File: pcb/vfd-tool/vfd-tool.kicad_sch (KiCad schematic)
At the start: 169 parts, among them J1 Conn_ARM_SWD_TagConnect_TC203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, J2 USB_C_Receptacle_USB2.0, J3 Micro_SD_Card, J4 Conn_01x10, J5 Raspberry_Pi_2_3, J6 Conn_02x15_Odd_Even, J7 Conn_02x15_Odd_Even, J8 Conn_02x08_Odd_Even, J9 Conn_01x02_Socket, SW1 SW_Push, SW2 SW_Push, U1 RP2040, U10 TPS54331DR, U11 BQ24075RGT, U2 USB2514B_M2, U3 SRV05-4, U4 FUSB302BMPX, U5 PCF85263AT, U6 W25Q32JVSS, U7 TPS562200, U8 TPS562200, U9 MAX17048G_T10, Y1 24MHz, Y2 24MHz, Y3 32.768kHz

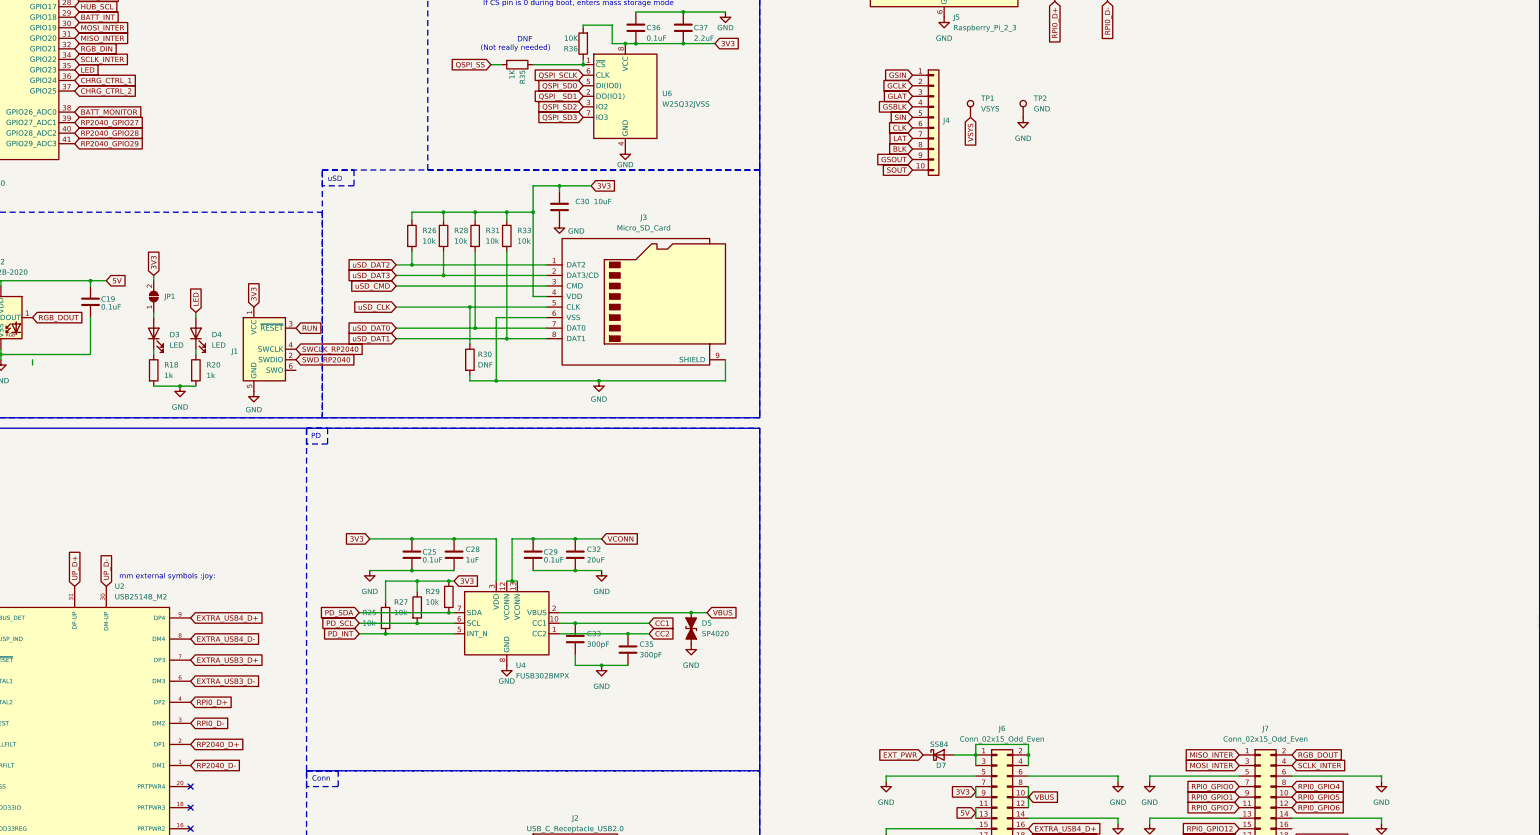
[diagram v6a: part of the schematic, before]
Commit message: DRC Fixed and added solder jumpers
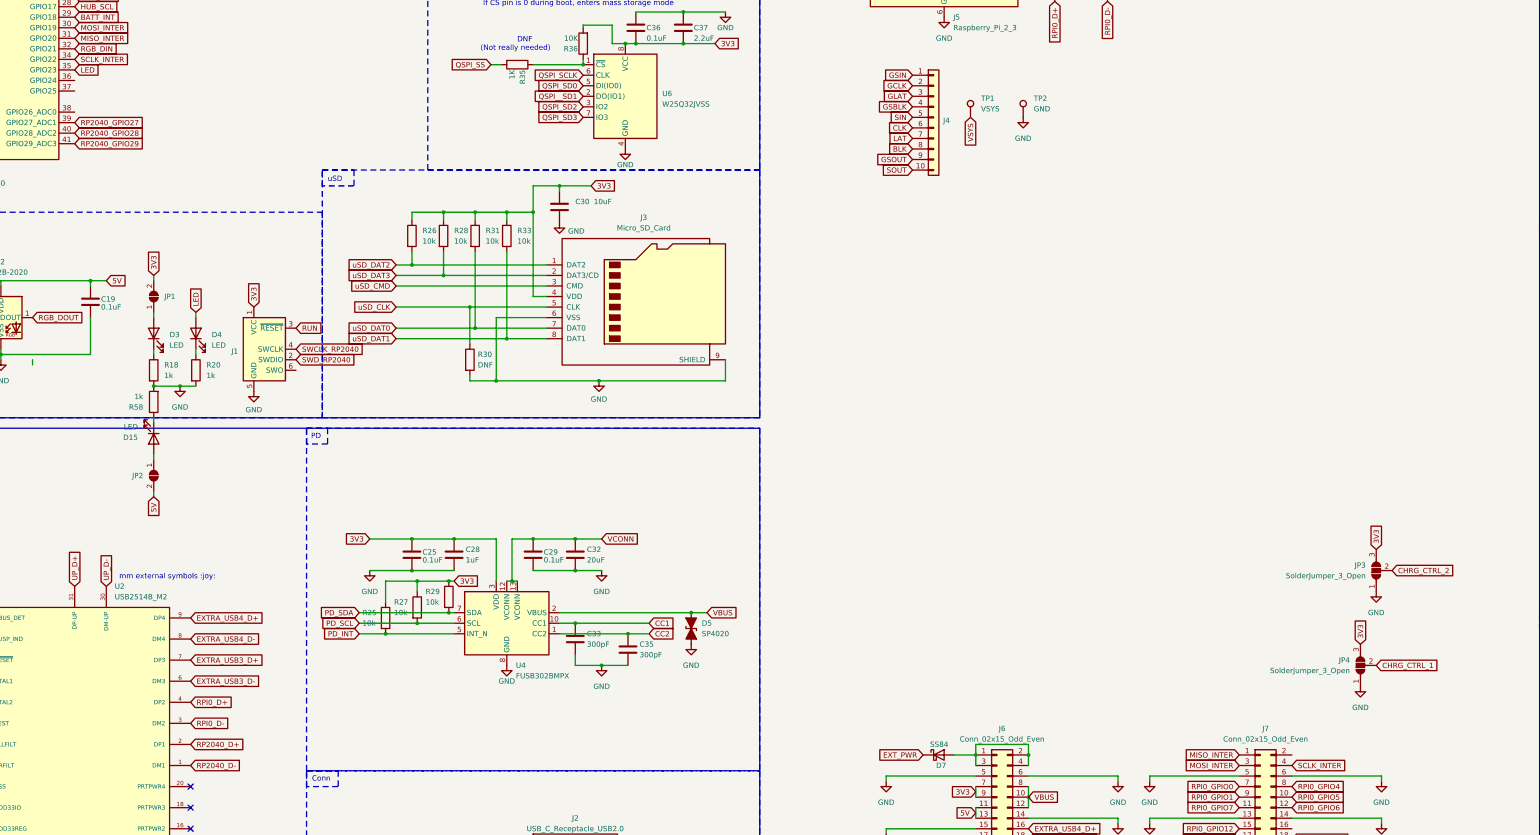
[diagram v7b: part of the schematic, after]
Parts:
- added D15: LED, LED_SMD:LED_0603_1608Metric, symbol Device:LED
- added JP2: SolderJumper_2_Open, Jumper:SolderJumper-2_P1.3mm_Open_TrianglePad1.0x1.5mm, symbol Jumper:SolderJumper_2_Open
- added JP3, JP4: SolderJumper_3_Open, Jumper:SolderJumper-3_P2.0mm_Open_TrianglePad1.0x1.5mm, symbol Jumper:SolderJumper_3_Open
- added R58: 1k, Resistor_SMD:R_0402_1005Metric, symbol Device:R
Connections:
- net 3V3: now also JP3.3 (B), JP4.3 (B)
- net 5V: now also JP2.2 (B)
- net BATT_MONITOR: no longer U1.38 (GPIO26_ADC0)
- net CHRG_CTRL_1: now also JP4.2 (C); no longer U1.36 (GPIO24)
- net CHRG_CTRL_2: now also JP3.2 (C); no longer U1.37 (GPIO25)
- net GND: now also JP3.1 (A), JP4.1 (A), R58.2
- net RGB_DOUT: no longer J7.2 (Pin_2)
- new net: D15.1 (K), R58.1
- new net: D15.2 (A), JP2.1 (A)

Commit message: fix #1 and #2
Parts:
- D11: value LED -> Blue
- D12, D15, D3: value LED -> Green
- D4: value LED -> Purple
- Y3: value 32.768kHz -> 32.768kHz
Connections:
- net GND: now also D10.2 (A), D5.2 (A2); no longer D10.1 (K), D5.1 (A1)
- net VBUS: now also D5.1 (A1); no longer D5.2 (A2)
- net at C46.1, L3.1, U10.8 (PH): now also D10.1 (K); no longer D10.2 (A)
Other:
- note added: "SP4020-01FTG"
- moved on the sheet: D10, JP3
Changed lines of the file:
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@@
 	)
 	(junction
-		(at 247.65 237.49)
-		(diameter 0)
-		(color 0 0 0 0)
-	)
-	(junction
 		(at 392.43 304.8)
 		(diameter 0)
@@
 	)
 	(junction
-		(at 527.05 95.25)
-		(diameter 0)
-		(color 0 0 0 0)
-	)
-	(junction
 		(at 547.37 102.87)
 		(diameter 0)
@@
 	)
 	(junction
+		(at 527.05 95.25)
+		(diameter 0)
+		(color 0 0 0 0)
+	)
+	(junction
 		(at 90.17 24.13)
 		(diameter 0)
@@
 	)
 	(junction
+		(at 247.65 237.49)
+		(diameter 0)
+		(color 0 0 0 0)
+	)
+	(junction
 		(at 504.19 182.88)
 		(diameter 0)
@@
 	(wire
 		(pts
+			(xy 247.65 237.49) (xy 251.46 237.49)
+		)
+		(stroke
+			(width 0)
+			(type default)
+		)
+	)
+	(wire
+		(pts
 			(xy 90.17 31.75) (xy 100.33 31.75)
 		)
@@
 	(wire
 		(pts
+			(xy 527.05 95.25) (xy 530.86 95.25)
+		)
+		(stroke
+			(width 0)
+			(type default)
+		)
+	)
+	(wire
+		(pts
 			(xy 328.93 295.91) (xy 328.93 297.18)
 		)
@@
 	(wire
 		(pts
-			(xy 247.65 237.49) (xy 215.9 237.49)
-		)
-		(stroke
-			(width 0)
-			(type default)
-		)
-	)
-	(wire
-		(pts
 			(xy 36.195 24.765) (xy 38.735 24.765)
 		)
@@
 	(wire
 		(pts
-			(xy 251.46 237.49) (xy 247.65 237.49)
+			(xy 215.9 237.49) (xy 247.65 237.49)
 		)
 		(stroke
@@
 	(wire
 		(pts
-			(xy 527.05 95.25) (xy 530.86 95.25)
-		)
-		(stroke
-			(width 0)
-			(type default)
-		)
-	)
-	(wire
-		(pts
 			(xy 195.58 140.97) (xy 203.2 140.97)
 		)
@@
 		)
 	)
+	(text "SP4020-01FTG"
+		(exclude_from_sim no)
+		(at 257.556 245.11 0)
+		(effects
+			(font
+				(size 1.27 1.27)
+			)
+		)
+	)
 	(text "TODO:\n1. Optimize power topology\n2. Fix calculated values\n3. add a step-up incase the EXT_PWR is below 5V"
 		(exclude_from_sim no)
@@
 	(global_label "CHRG_CTRL_2"
 		(shape input)
-		(at 416.56 227.33 0)
+		(at 412.75 226.06 0)
 		(fields_autoplaced yes)
 		(effects
@@
 		)
 		(property "Intersheetrefs" "${INTERSHEET_REFS}"
-			(at 432.3661 227.33 0)
+			(at 428.5561 226.06 0)
 			(effects
 				(font
@@
 	(global_label "3V3"
 		(shape input)
-		(at 412.75 222.25 90)
+		(at 408.94 220.98 90)
 		(fields_autoplaced yes)
 		(effects
@@
 		)
 		(property "Intersheetrefs" "${INTERSHEET_REFS}"
-			(at 412.75 215.7572 90)
+			(at 408.94 214.4872 90)
 			(effects
 				(font
@@
 			)
 		)
-		(property "Value" "LED"
+		(property "Value" "Green"
 			(at 121.92 173.0375 90)
 			(effects
@@
 	)
 	(symbol
+		(lib_id "Device:D_TVS_Filled")
+		(at 247.65 241.3 270)
+		(unit 1)
+		(exclude_from_sim no)
+		(in_bom yes)
+		(on_board yes)
+		(dnp no)
+		(fields_autoplaced yes)
+		(property "Reference" "D5"
+			(at 250.19 240.0299 90)
+			(effects
+				(font
+					(size 1.27 1.27)
+				)
+				(justify left)
+			)
+		)
+		(property "Value" "SP4020"
+			(at 250.19 242.5699 90)
+			(effects
+				(font
+					(size 1.27 1.27)
+				)
+				(justify left)
+			)
+		)
+		(property "Footprint" "Diode_SMD:D_SOD-323"
+			(at 247.65 241.3 0)
+			(effects
+				(font
+					(size 1.27 1.27)
+				)
+				(hide yes)
+			)
+		)
+		(property "Datasheet" "~"
+			(at 247.65 241.3 0)
+			(effects
+				(font
+					(size 1.27 1.27)
+				)
+				(hide yes)
+			)
+		)
+		(property "Description" "Bidirectional transient-voltage-suppression diode, filled shape"
+			(at 247.65 241.3 0)
+			(effects
+				(font
+					(size 1.27 1.27)
+				)
+				(hide yes)
+			)
+		)
+		(pin "1"
+		)
+		(pin "2"
+		)
+		(instances
+			(project "vfd-tool"
+				(path "/849d9919-4175-4212-8785-6cd0421cfa2d"
+					(reference "D5")
+					(unit 1)
+				)
+			)
+		)
+	)
+	(symbol
 		(lib_id "MAX17048G_T10:MAX17048G_T10")
 		(at 514.35 260.35 0)
@@
 			)
 		)
-		(property "Value" "LED"
+		(property "Value" "Purple"
 			(at 132.08 173.0375 90)
 			(effects
@@
 		(on_board yes)
 		(dnp no)
-		(fields_autoplaced yes)
 		(property "Reference" "D12"
-			(at 545.7825 190.5 0)
+			(at 547.37 190.5 0)
 			(effects
 				(font
@@
 			)
 		)
-		(property "Value" "LED"
-			(at 545.7825 193.04 0)
+		(property "Value" "Green"
+			(at 547.37 193.04 0)
 			(effects
 				(font
@@
 	(symbol
 		(lib_id "power:GND")
-		(at 412.75 232.41 0)
+		(at 408.94 231.14 0)
 		(unit 1)
 		(exclude_from_sim no)
@@
 		(fields_autoplaced yes)
 		(property "Reference" "#PWR066"
-			(at 412.75 238.76 0)
+			(at 408.94 237.49 0)
 			(effects
 				(font
@@
 		)
 		(property "Value" "GND"
-			(at 412.75 237.49 0)
+			(at 408.94 236.22 0)
 			(effects
 				(font
@@
 		)
 		(property "Footprint" ""
-			(at 412.75 232.41 0)
+			(at 408.94 231.14 0)
 			(effects
 				(font
@@
 		)
 		(property "Datasheet" ""
-			(at 412.75 232.41 0)
+			(at 408.94 231.14 0)
 			(effects
 				(font
@@
 		)
 		(property "Description" ""
-			(at 412.75 232.41 0)
+			(at 408.94 231.14 0)
 			(effects
 				(font
@@
 			)
 		)
-		(property "Value" "32.768kHz "
+		(property "Value" "32.768kHz"
 			(at 199.39 62.2299 90)
 			(effects
@@
 			)
 		)
-		(property "Value" "LED"
+		(property "Value" "Green"
 			(at 114.3 192.7225 90)
 			(effects
@@
 	(symbol
 		(lib_id "Device:D_Schottky")
-		(at 527.05 99.06 90)
+		(at 527.05 99.06 270)
 		(unit 1)
 		(exclude_from_sim no)
@@
 		(dnp no)
 		(property "Reference" "D10"
-			(at 529.844 97.028 0)
+			(at 524.256 101.092 0)
 			(effects
 				(font
@@
 		)
 		(property "Value" "CMS04"
-			(at 532.13 95.758 0)
+			(at 521.97 102.362 0)
 			(effects
 				(font
@@
 	)
 	(symbol
-		(lib_id "Device:D_TVS_Filled")
-		(at 247.65 241.3 90)
-		(unit 1)
-		(exclude_from_sim no)
-		(in_bom yes)
-		(on_board yes)
-		(dnp no)
-		(fields_autoplaced yes)
-		(property "Reference" "D5"
-			(at 250.19 240.0299 90)
-			(effects
-				(font
-					(size 1.27 1.27)
-				)
-				(justify right)
-			)
-		)
-		(property "Value" "SP4020"
-			(at 250.19 242.5699 90)
-			(effects
-				(font
-					(size 1.27 1.27)
-				)
-				(justify right)
-			)
-		)
-		(property "Footprint" "Diode_SMD:D_SOD-323"
-			(at 247.65 241.3 0)
-			(effects
-				(font
-					(size 1.27 1.27)
-				)
-				(hide yes)
-			)
-		)
-		(property "Datasheet" "~"
-			(at 247.65 241.3 0)
-			(effects
-				(font
-					(size 1.27 1.27)
-				)
-				(hide yes)
-			)
-		)
-		(property "Description" "Bidirectional transient-voltage-suppression diode, filled shape"
-			(at 247.65 241.3 0)
-			(effects
-				(font
-					(size 1.27 1.27)
-				)
-				(hide yes)
-			)
-		)
-		(pin "1"
-		)
-		(pin "2"
-		)
-		(instances
-			(project "vfd-tool"
-				(path "/849d9919-4175-4212-8785-6cd0421cfa2d"
-					(reference "D5")
-					(unit 1)
-				)
-			)
-		)
-	)
-	(symbol
 		(lib_name "GND_17")
 		(lib_id "power:GND")
@@
 	(symbol
 		(lib_id "Jumper:SolderJumper_3_Open")
-		(at 412.75 227.33 90)
+		(at 408.94 226.06 90)
 		(unit 1)
 		(exclude_from_sim yes)
@@
 		(fields_autoplaced yes)
 		(property "Reference" "JP3"
-			(at 410.21 226.0599 90)
+			(at 406.4 224.7899 90)
 			(effects
 				(font
@@
 		)
 		(property "Value" "SolderJumper_3_Open"
-			(at 410.21 228.5999 90)
+			(at 406.4 227.3299 90)
 			(effects
 				(font
@@
 		)
 		(property "Footprint" "Jumper:SolderJumper-3_P2.0mm_Open_TrianglePad1.0x1.5mm"
-			(at 412.75 227.33 0)
+			(at 408.94 226.06 0)
 			(effects
 				(font
@@
 		)
 		(property "Datasheet" "~"
-			(at 412.75 227.33 0)
+			(at 408.94 226.06 0)
 			(effects
 				(font
@@
 		)
 		(property "Description" "Solder Jumper, 3-pole, open"
-			(at 412.75 227.33 0)
+			(at 408.94 226.06 0)
 			(effects
 				(font
@@
 		(on_board yes)
 		(dnp no)
-		(fields_autoplaced yes)
 		(property "Reference" "D11"
-			(at 539.4325 198.12 0)
+			(at 540.004 198.12 0)
 			(effects
 				(font
@@
 			)
 		)
-		(property "Value" "LED"
-			(at 539.4325 200.66 0)
+		(property "Value" "Blue"
+			(at 540.004 200.66 0)
 			(effects
 				(font
